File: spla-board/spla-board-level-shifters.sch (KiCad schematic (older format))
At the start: 22 parts, among them J6 J_BODGE, J7 J_SAMPLE, U15 74LVC8T245, U16 74LVC8T245, U17 74LVC8T245, U20 74LVC8T245, U22 74LVC8T245, U23 74LVC8T245, U24 74LVC8T245, U25 74LVC8T245, U26 74LVC8T245, U27 74LVC8T245, U28 74LVC8T245, U29 74LVC8T245, U30 74LVC8T245, U31 74LVC8T245, U32 74LVC8T245

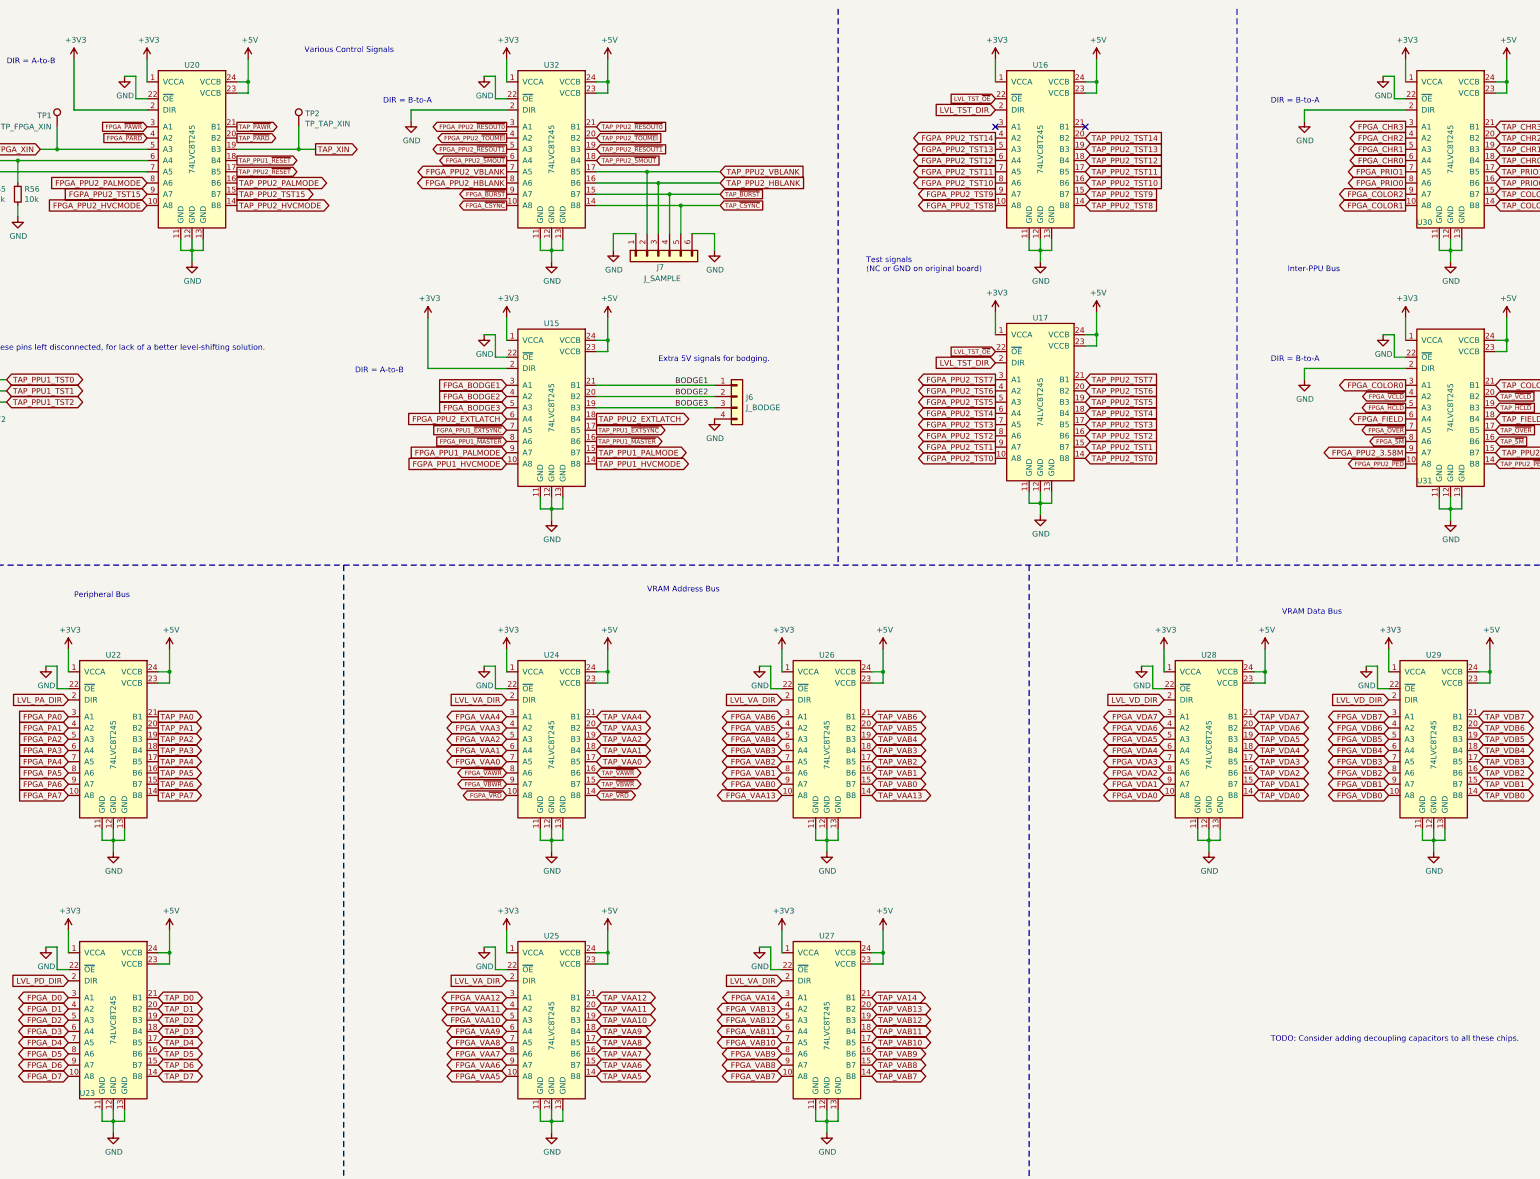
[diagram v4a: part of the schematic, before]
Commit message: schematic/pcb: Renumber level shifters.
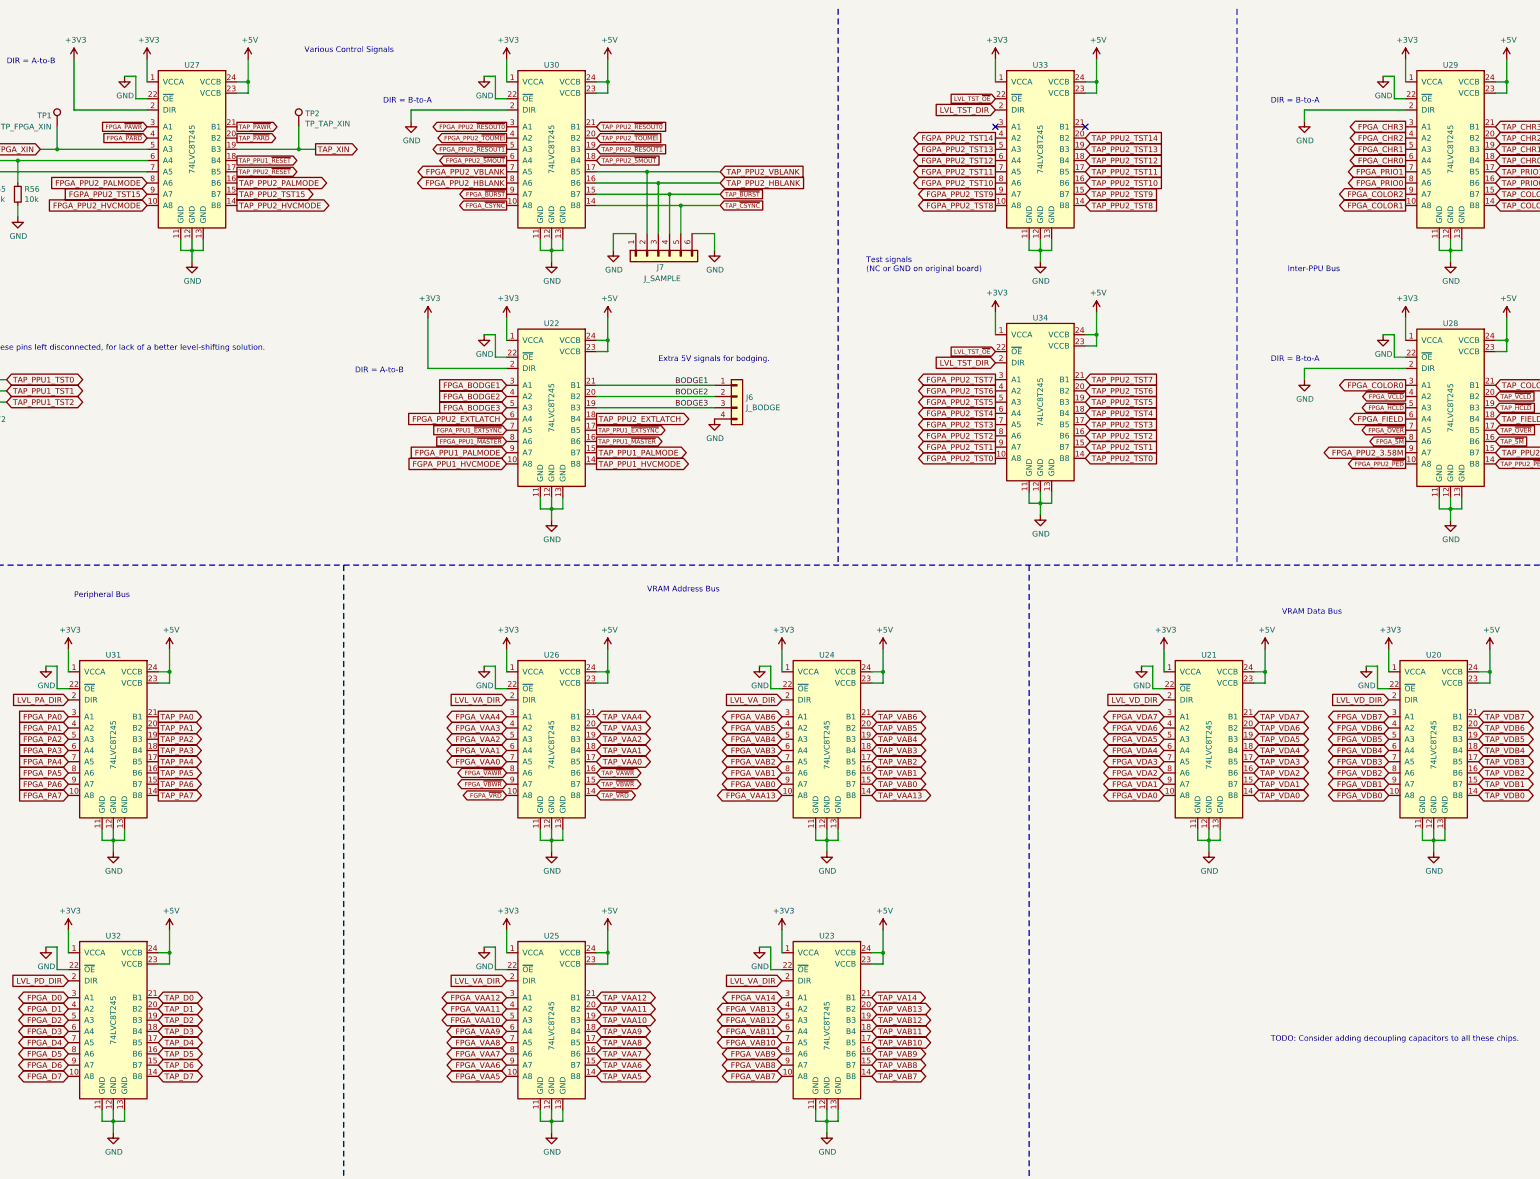
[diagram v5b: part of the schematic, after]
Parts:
- renumbered U29 to U20, U28 to U21, U15 to U22, U27 to U23, U26 to U24, U24 to U26, U20 to U27, U31 to U28, U30 to U29, U32 to U30, U22 to U31, U23 to U32, U16 to U33, U17 to U34
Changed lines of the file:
@@
 FPGA_~PAWR~
 $Comp
-L SPLA:74LVC8T245 U23
+L SPLA:74LVC8T245 U32
 U 1 1 5E550799
 P 2400 9500
-F 0 "U23" H 2100 8850 50  0000 L CNN
+F 0 "U32" H 2400 10250 50  0000 C CNN
 F 1 "74LVC8T245" V 2400 9500 50  0000 C CNN
 F 2 "Package_SO:TSSOP-24_4.4x7.8mm_P0.65mm" H 2400 8750 50  0001 C CNN
@@
 $EndComp
 $Comp
-L SPLA:74LVC8T245 U22
+L SPLA:74LVC8T245 U31
 U 1 1 5E55EB1D
 P 2400 7000
-F 0 "U22" H 2400 7750 50  0000 C CNN
+F 0 "U31" H 2400 7750 50  0000 C CNN
 F 1 "74LVC8T245" V 2400 6950 50  0000 C CNN
 F 2 "Package_SO:TSSOP-24_4.4x7.8mm_P0.65mm" H 2400 5700 50  0001 C CNN
@@
 FPGA_PA7
 $Comp
-L SPLA:74LVC8T245 U26
+L SPLA:74LVC8T245 U24
 U 1 1 5E56FCA9
 P 8750 7000
-F 0 "U26" H 8750 7750 50  0000 C CNN
+F 0 "U24" H 8750 7750 50  0000 C CNN
 F 1 "74LVC8T245" V 8750 6950 50  0000 C CNN
 F 2 "Package_SO:TSSOP-24_4.4x7.8mm_P0.65mm" H 8750 5700 50  0001 C CNN
@@
 Peripheral Bus
 $Comp
-L SPLA:74LVC8T245 U24
+L SPLA:74LVC8T245 U26
 U 1 1 5E5C1563
 P 6300 7000
-F 0 "U24" H 6300 7750 50  0000 C CNN
+F 0 "U26" H 6300 7750 50  0000 C CNN
 F 1 "74LVC8T245" V 6300 6950 50  0000 C CNN
 F 2 "Package_SO:TSSOP-24_4.4x7.8mm_P0.65mm" H 6300 5700 50  0001 C CNN
@@
 TAP_~VBWR~
 $Comp
-L SPLA:74LVC8T245 U28
+L SPLA:74LVC8T245 U21
 U 1 1 5E61780A
 P 12150 7000
-F 0 "U28" H 12150 7750 50  0000 C CNN
+F 0 "U21" H 12150 7750 50  0000 C CNN
 F 1 "74LVC8T245" V 12150 6950 50  0000 C CNN
 F 2 "Package_SO:TSSOP-24_4.4x7.8mm_P0.65mm" H 12150 5700 50  0001 C CNN
@@
 FPGA_VDB7
 $Comp
-L SPLA:74LVC8T245 U29
+L SPLA:74LVC8T245 U20
 U 1 1 5E61D896
 P 14150 7000
-F 0 "U29" H 14150 7750 50  0000 C CNN
+F 0 "U20" H 14150 7750 50  0000 C CNN
 F 1 "74LVC8T245" V 14150 6950 50  0000 C CNN
 F 2 "Package_SO:TSSOP-24_4.4x7.8mm_P0.65mm" H 14150 5700 50  0001 C CNN
@@
 FPGA_CHR3
 $Comp
-L SPLA:74LVC8T245 U30
+L SPLA:74LVC8T245 U29
 U 1 1 5E65F50D
 P 14300 1750
-F 0 "U30" H 14000 1100 50  0000 L CNN
+F 0 "U29" H 14300 2500 50  0000 C CNN
 F 1 "74LVC8T245" V 14300 1750 50  0000 C CNN
 F 2 "Package_SO:TSSOP-24_4.4x7.8mm_P0.65mm" H 14300 1000 50  0001 C CNN
@@
 Inter-PPU Bus\n
 $Comp
-L SPLA:74LVC8T245 U31
+L SPLA:74LVC8T245 U28
 U 1 1 5E66CF65
 P 14300 4050
-F 0 "U31" H 14000 3400 50  0000 L CNN
+F 0 "U28" H 14300 4800 50  0000 C CNN
 F 1 "74LVC8T245" V 14300 4050 50  0000 C CNN
 F 2 "Package_SO:TSSOP-24_4.4x7.8mm_P0.65mm" H 14300 3300 50  0001 C CNN
@@
 TAP_PPU2_TST15
 $Comp
-L SPLA:74LVC8T245 U16
+L SPLA:74LVC8T245 U33
 U 1 1 5E8BF4CB
 P 10650 1750
-F 0 "U16" H 10650 2500 50  0000 C CNN
+F 0 "U33" H 10650 2500 50  0000 C CNN
 F 1 "74LVC8T245" V 10650 1750 50  0000 C CNN
 F 2 "Package_SO:TSSOP-24_4.4x7.8mm_P0.65mm" H 10650 1000 50  0001 C CNN
@@
 $EndComp
 $Comp
-L SPLA:74LVC8T245 U17
+L SPLA:74LVC8T245 U34
 U 1 1 5E8C0531
 P 10650 4000
-F 0 "U17" H 10650 4750 50  0000 C CNN
+F 0 "U34" H 10650 4750 50  0000 C CNN
 F 1 "74LVC8T245" V 10650 4000 50  0000 C CNN
 F 2 "Package_SO:TSSOP-24_4.4x7.8mm_P0.65mm" H 10650 3250 50  0001 C CNN
@@
 TAP_PPU2_EXTLATCH
 $Comp
-L SPLA:74LVC8T245 U32
+L SPLA:74LVC8T245 U30
 U 1 1 5E6DACCD
 P 6300 1750
-F 0 "U32" H 6300 2500 50  0000 C CNN
+F 0 "U30" H 6300 2500 50  0000 C CNN
 F 1 "74LVC8T245" V 6300 1750 50  0000 C CNN
 F 2 "Package_SO:TSSOP-24_4.4x7.8mm_P0.65mm" H 6300 1000 50  0001 C CNN
@@
 $EndComp
 $Comp
-L SPLA:74LVC8T245 U15
+L SPLA:74LVC8T245 U22
 U 1 1 5E8C1D06
 P 6300 4050
-F 0 "U15" H 6300 4800 50  0000 C CNN
+F 0 "U22" H 6300 4800 50  0000 C CNN
 F 1 "74LVC8T245" V 6300 4050 50  0000 C CNN
 F 2 "Package_SO:TSSOP-24_4.4x7.8mm_P0.65mm" H 6300 3300 50  0001 C CNN
@@
 FPGA_BODGE3
 $Comp
-L SPLA:74LVC8T245 U20
+L SPLA:74LVC8T245 U27
 U 1 1 5E517B3B
 P 3100 1750
-F 0 "U20" H 3100 2500 50  0000 C CNN
+F 0 "U27" H 3100 2500 50  0000 C CNN
 F 1 "74LVC8T245" V 3100 1750 50  0000 C CNN
 F 2 "Package_SO:TSSOP-24_4.4x7.8mm_P0.65mm" H 3100 1000 50  0001 C CNN
@@
 	10550 5450 10550 11200
 $Comp
-L SPLA:74LVC8T245 U27
+L SPLA:74LVC8T245 U23
 U 1 1 5E5DCE42
 P 8750 9500
-F 0 "U27" H 8750 10250 50  0000 C CNN
+F 0 "U23" H 8750 10250 50  0000 C CNN
 F 1 "74LVC8T245" V 8750 9450 50  0000 C CNN
 F 2 "Package_SO:TSSOP-24_4.4x7.8mm_P0.65mm" H 8750 8200 50  0001 C CNN

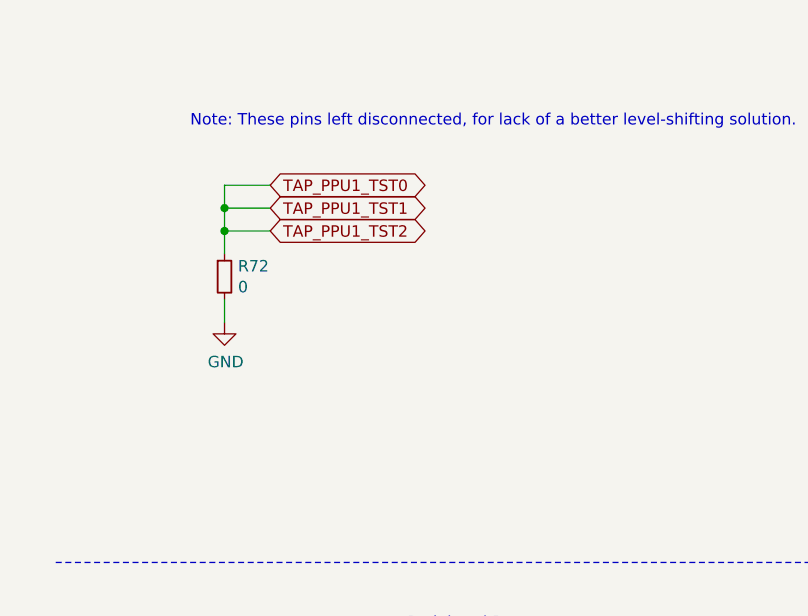
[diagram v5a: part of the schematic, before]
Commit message: schematic/pcb: Seperate PPU2 AVCC; add more PPU decoupling.
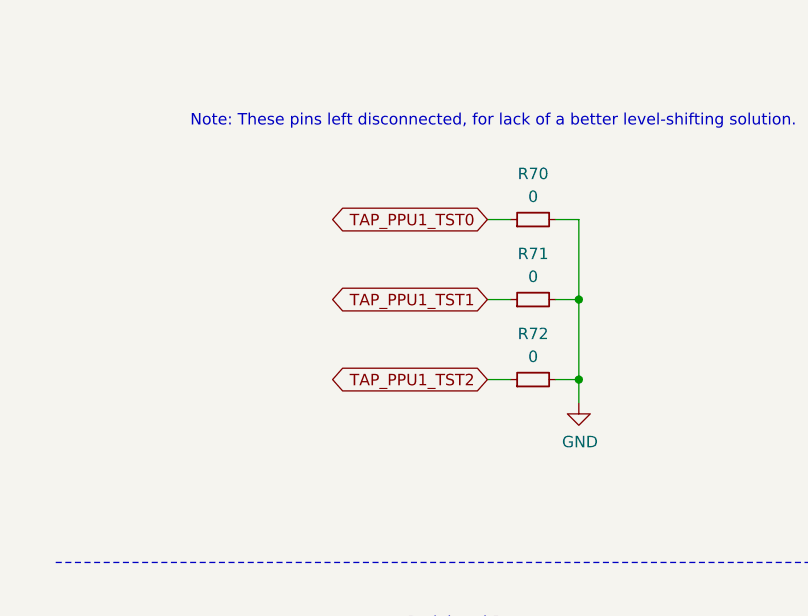
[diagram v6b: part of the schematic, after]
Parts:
- added R71, R72: 0, Resistor_SMD:R_0603_1608Metric, symbol Device:R_Small
- renumbered R72 to R70
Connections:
- net GND: now also R71.2, R72.2
- new net TAP_PPU1_TST1: R71.1
- new net TAP_PPU1_TST2: R72.1
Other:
- moved on the sheet: R70
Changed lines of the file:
@@
 Text GLabel 2800 6800 2    50   Output ~ 0
 TAP_PA0
-Text GLabel 1450 3800 2    50   BiDi ~ 0
+Text GLabel 2400 3950 0    50   BiDi ~ 0
 TAP_PPU1_TST0
-Text GLabel 1450 3900 2    50   BiDi ~ 0
+Text GLabel 2400 4300 0    50   BiDi ~ 0
 TAP_PPU1_TST1
-Text GLabel 1450 4000 2    50   BiDi ~ 0
+Text GLabel 2400 4650 0    50   BiDi ~ 0
 TAP_PPU1_TST2
 Text GLabel 11050 4500 2    50   Input ~ 0
@@
 	11150 1150 11150 1250
 Wire Wire Line
-	1250 3800 1450 3800
-Wire Wire Line
-	1250 3900 1450 3900
-Wire Wire Line
-	1250 4000 1450 4000
-Wire Wire Line
 	4050 1750 3500 1750
 Connection ~ 4050 1750
@@
 DIR = B-to-A
 $Comp
-L Device:R_Small R72
+L Device:R_Small R70
 U 1 1 5F2D13A9
-P 1250 4200
-F 0 "R72" H 1309 4246 50  0000 L CNN
-F 1 "0" H 1309 4155 50  0000 L CNN
-F 2 "Resistor_SMD:R_0603_1608Metric" H 1250 4200 50  0001 C CNN
-F 3 "~" H 1250 4200 50  0001 C CNN
-F 4 "2019-RK73Z1JTTDCT-ND" H 1250 4200 50  0001 C CNN "Digikey"
-F 5 "KOA Speer Electronics Inc." H 1250 4200 50  0001 C CNN "Manufacturer"
-F 6 "RK73Z1JTTD" H 1250 4200 50  0001 C CNN "Manufacturer Id"
-	1    1250 4200
-	1    0    0    -1
+P 2600 3950
+F 0 "R70" V 2800 3950 50  0000 C CNN
+F 1 "0" V 2700 3950 50  0000 C CNN
+F 2 "Resistor_SMD:R_0603_1608Metric" H 2600 3950 50  0001 C CNN
+F 3 "~" H 2600 3950 50  0001 C CNN
+F 4 "2019-RK73Z1JTTDCT-ND" H 2600 3950 50  0001 C CNN "Digikey"
+F 5 "KOA Speer Electronics Inc." H 2600 3950 50  0001 C CNN "Manufacturer"
+F 6 "RK73Z1JTTD" H 2600 3950 50  0001 C CNN "Manufacturer Id"
+	1    2600 3950
+	0    -1   -1   0
 $EndComp
 $Comp
 L power:GND #PWR011
 U 1 1 5F2D1E97
-P 1250 4400
-F 0 "#PWR011" H 1250 4150 50  0001 C CNN
-F 1 "GND" H 1255 4227 50  0000 C CNN
-F 2 "" H 1250 4400 50  0001 C CNN
-F 3 "" H 1250 4400 50  0001 C CNN
-	1    1250 4400
-	1    0    0    -1
-$EndComp
-Wire Wire Line
-	1250 3800 1250 3900
-Connection ~ 1250 3900
-Wire Wire Line
-	1250 3900 1250 4000
-Connection ~ 1250 4000
-Wire Wire Line
-	1250 4000 1250 4100
-Wire Wire Line
-	1250 4300 1250 4400
+P 2800 4750
+F 0 "#PWR011" H 2800 4500 50  0001 C CNN
+F 1 "GND" H 2805 4577 50  0000 C CNN
+F 2 "" H 2800 4750 50  0001 C CNN
+F 3 "" H 2800 4750 50  0001 C CNN
+	1    2800 4750
+	1    0    0    -1
+$EndComp
 Wire Notes Line
 	10550 5450 10550 11200
@@
 Wire Wire Line
 	6850 2500 6850 2650
+$Comp
+L Device:R_Small R71
+U 1 1 5F54AD0D
+P 2600 4300
+F 0 "R71" V 2800 4300 50  0000 C CNN
+F 1 "0" V 2700 4300 50  0000 C CNN
+F 2 "Resistor_SMD:R_0603_1608Metric" H 2600 4300 50  0001 C CNN
+F 3 "~" H 2600 4300 50  0001 C CNN
+F 4 "2019-RK73Z1JTTDCT-ND" H 2600 4300 50  0001 C CNN "Digikey"
+F 5 "KOA Speer Electronics Inc." H 2600 4300 50  0001 C CNN "Manufacturer"
+F 6 "RK73Z1JTTD" H 2600 4300 50  0001 C CNN "Manufacturer Id"
+	1    2600 4300
+	0    -1   -1   0
+$EndComp
+$Comp
+L Device:R_Small R72
+U 1 1 5F55CC77
+P 2600 4650
+F 0 "R72" V 2800 4650 50  0000 C CNN
+F 1 "0" V 2700 4650 50  0000 C CNN
+F 2 "Resistor_SMD:R_0603_1608Metric" H 2600 4650 50  0001 C CNN
+F 3 "~" H 2600 4650 50  0001 C CNN
+F 4 "2019-RK73Z1JTTDCT-ND" H 2600 4650 50  0001 C CNN "Digikey"
+F 5 "KOA Speer Electronics Inc." H 2600 4650 50  0001 C CNN "Manufacturer"
+F 6 "RK73Z1JTTD" H 2600 4650 50  0001 C CNN "Manufacturer Id"
+	1    2600 4650
+	0    -1   -1   0
+$EndComp
+Wire Wire Line
+	2400 3950 2500 3950
+Wire Wire Line
+	2500 4300 2400 4300
+Wire Wire Line
+	2400 4650 2500 4650
+Wire Wire Line
+	2700 3950 2800 3950
+Wire Wire Line
+	2800 3950 2800 4300
+Wire Wire Line
+	2700 4650 2800 4650
+Connection ~ 2800 4650
+Wire Wire Line
+	2800 4650 2800 4750
+Wire Wire Line
+	2700 4300 2800 4300
+Connection ~ 2800 4300
+Wire Wire Line
+	2800 4300 2800 4650
 $EndSCHEMATC
